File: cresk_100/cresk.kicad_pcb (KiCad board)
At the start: 2 copper layers, 100 x 100 mm, 52 parts, among them J1 8P8C, J2 8P8C, J3 Conn_01x05_Male, J4 Conn_01x05_Male, SW1 SW_Push, SW10 SW_Push, SW11 SW_Push, SW12 SW_Push, SW13 SW_Push, SW14 SW_Push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

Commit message: cresk_100: update through hole size
Pad size to 1.6 mm and drill to 1 mm.
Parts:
- moved J3 10.2 mm to (110.4, 56.8), turned to 0 degrees
- moved J4 10.2 mm to (82.5, 56.8), turned to 180 degrees

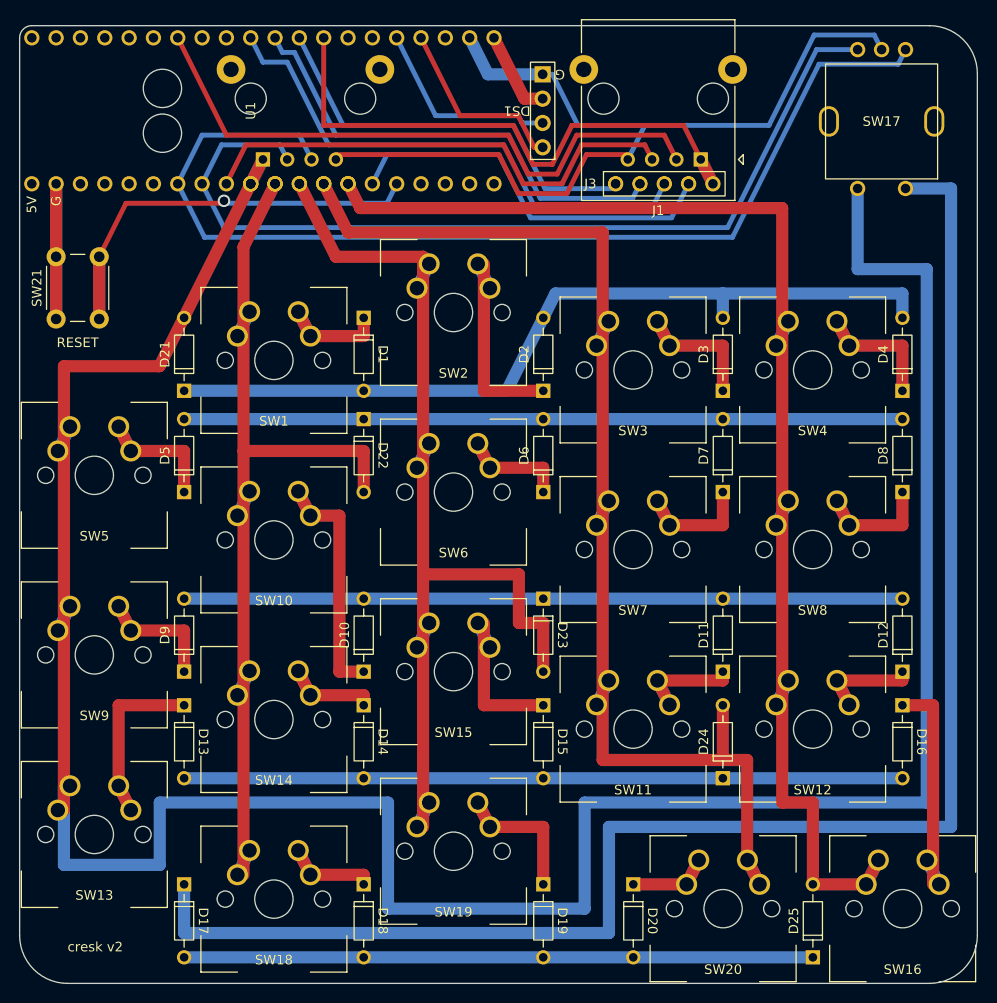
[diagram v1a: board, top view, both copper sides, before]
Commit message: cresk_100: change pin mapping
Make it compatible with non flipped BlackPill, and possibly ProMicro.
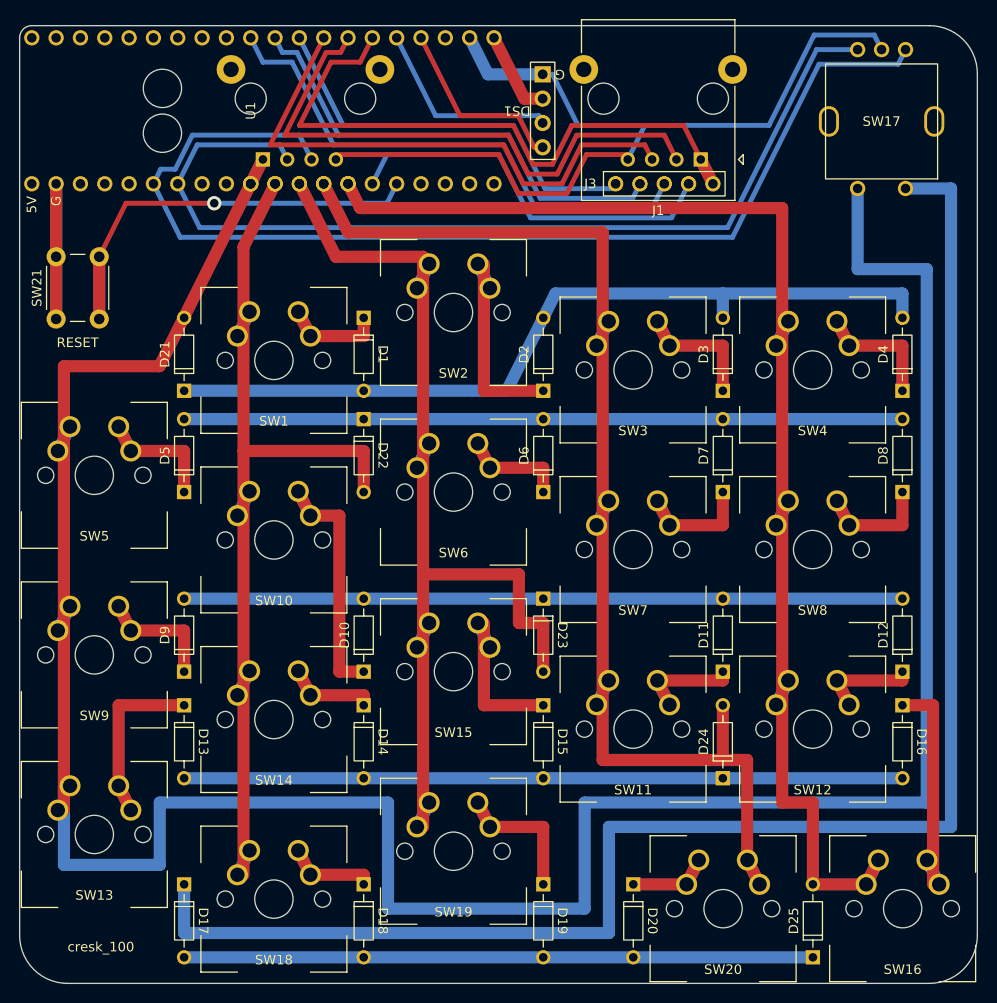
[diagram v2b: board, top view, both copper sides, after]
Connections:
- J3 pad 1: col9 -> col5
- J3 pad 2: col8 -> col6
- J3 pad 4: col6 -> col8
- J3 pad 5: col5 -> col9
- J4 pad 1: col0 -> col4
- J4 pad 2: col1 -> col3
- J4 pad 4: col3 -> col1
- J4 pad 5: col4 -> col0
- U1 pad 26: unconnected-(U1-Pad26) -> col9
- U1 pad 27: unconnected-(U1-Pad27) -> b2
- U1 pad 28: col9 -> a2
- U1 pad 34: b2 -> unconnected-(U1-Pad34)
- U1 pad 6: unconnected-(U1-Pad6) -> a1
- U1 pad 7: a1 -> b1
- U1 pad 8: b1 -> unconnected-(U1-Pad8)
- U1 pad 9: a2 -> unconnected-(U1-Pad9)
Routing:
- net col9: track 61.4 -> 68.1 mm
- net a2: track 52.9 -> 58.3 mm
- net a1: track 110.2 -> 115.3 mm
- net b1: track 95.1 -> 100.2 mm
- net b2: track 64.9 -> 60.4 mm
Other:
- board text added: "cresk_100"
- board text removed: "cresk v2"

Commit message: cresk_100: revert mx spacing to 19 mm
Was 18.75 mm. Works.
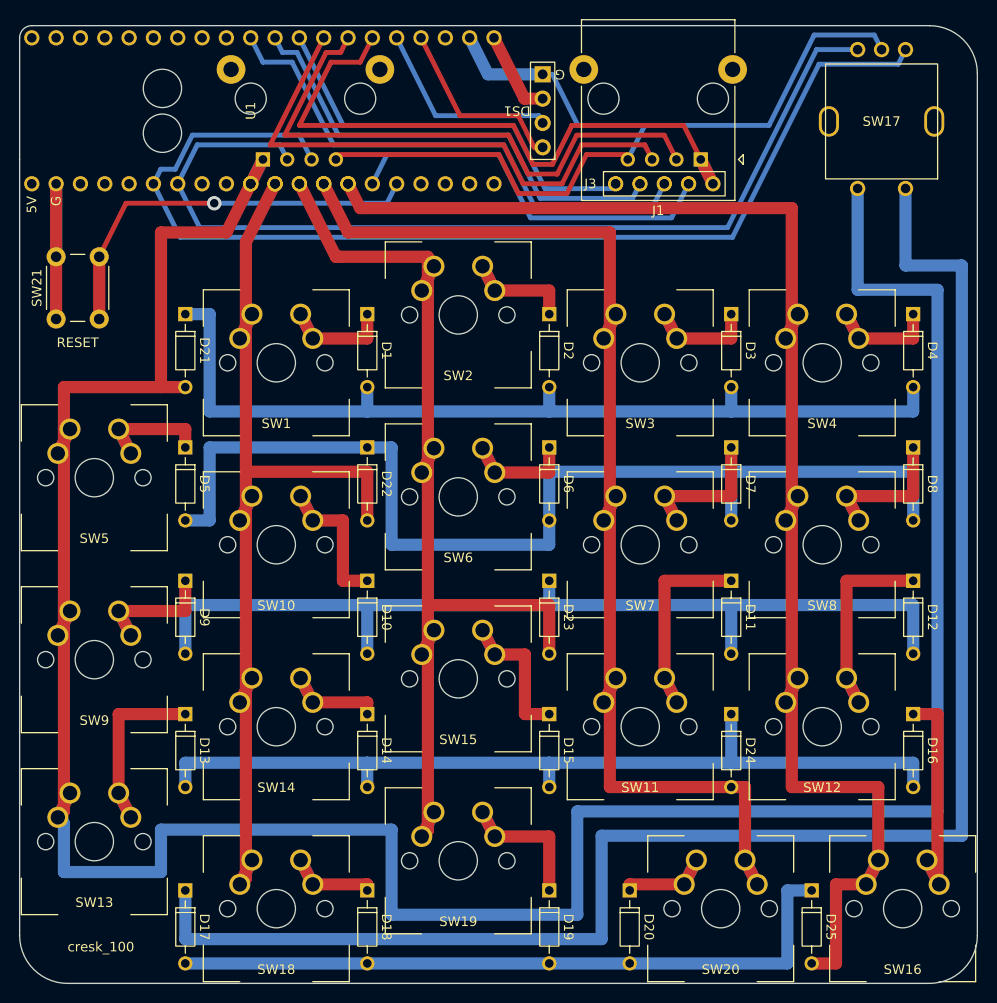
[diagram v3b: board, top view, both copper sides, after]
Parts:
- moved D12 9.56 mm to (141.5, 98.3), turned to -90 degrees
- moved D11 9.53 mm to (122.5, 98.3), turned to -90 degrees
- moved D10 9.50 mm to (84.5, 98.3), turned to -90 degrees
- moved D9 9.49 mm to (65.5, 98.3), turned to -90 degrees
- moved D4 8.08 mm to (141.5, 70.4), turned to -90 degrees
- moved D3 8.05 mm to (122.5, 70.4), turned to -90 degrees
- moved D2 8.03 mm to (103.5, 70.4), turned to -90 degrees
- moved D21 8.01 mm to (65.5, 70.4), turned to -90 degrees
- moved D25 6.99 mm to (130.9, 130.6), turned to -90 degrees
- moved D24 6.76 mm to (122.5, 112.2), turned to -90 degrees
- moved D8 4.79 mm to (141.5, 84.3), turned to -90 degrees
- moved D7 4.74 mm to (122.5, 84.3), turned to -90 degrees
- moved D6 4.70 mm to (103.5, 84.3), turned to -90 degrees
- moved D5 4.66 mm to (65.5, 84.3), turned to -90 degrees
- moved D22 2.98 mm to (84.5, 84.3)
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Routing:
- net row1: track 75.0 -> 111.6 mm
- net row2: track 75.0 -> 98.9 mm
- net col4: track 140.5 -> 161.7 mm
- net col0: track 287.3 -> 303.9 mm
- net row3: track 75.0 -> 91.2 mm
- net col1: track 101.1 -> 114.6 mm
- net row0: track 86.4 -> 96.3 mm
- net Net-(D10-Pad1): track 27.5 -> 17.7 mm
- net Net-(D11-Pad1): track 13.4 -> 22.8 mm
- net Net-(D12-Pad1): track 13.4 -> 22.8 mm
- net Net-(D2-Pad1): track 22.3 -> 13.8 mm
- net col2: track 111.2 -> 119.4 mm
- net row4: track 65.7 -> 73.0 mm
- net Net-(SW21-Pad2): track 48.8 -> 42.3 mm
- net GND: track 123.2 -> 116.7 mm
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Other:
- outline, holes or cut-outs redrawn
